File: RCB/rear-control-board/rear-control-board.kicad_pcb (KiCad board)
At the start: 2 copper layers, 99.1 x 99.1 mm, 55 parts, among them J1 Conn_01x23, J2 Conn_01x14, J3 Conn_01x08, J4 Conn_01x02, J5 Conn_01x02, J6 Conn_01x05, K1 T9VV1K15-12S, K2 G5V-2, K3 G5V-2, Q1 BSS84, Q2 2N7002, Q3 Q_PMOS_GDSD, Q4 Q_PMOS_GDSD, Q5 Q_PMOS_GDSD, U1 STM32F413CGUx, U2 LD1117S33TR_SOT223, U3 R-78B5.0-2.0, U4 MCP2551-I-SN, Y1 CSTNE8M00

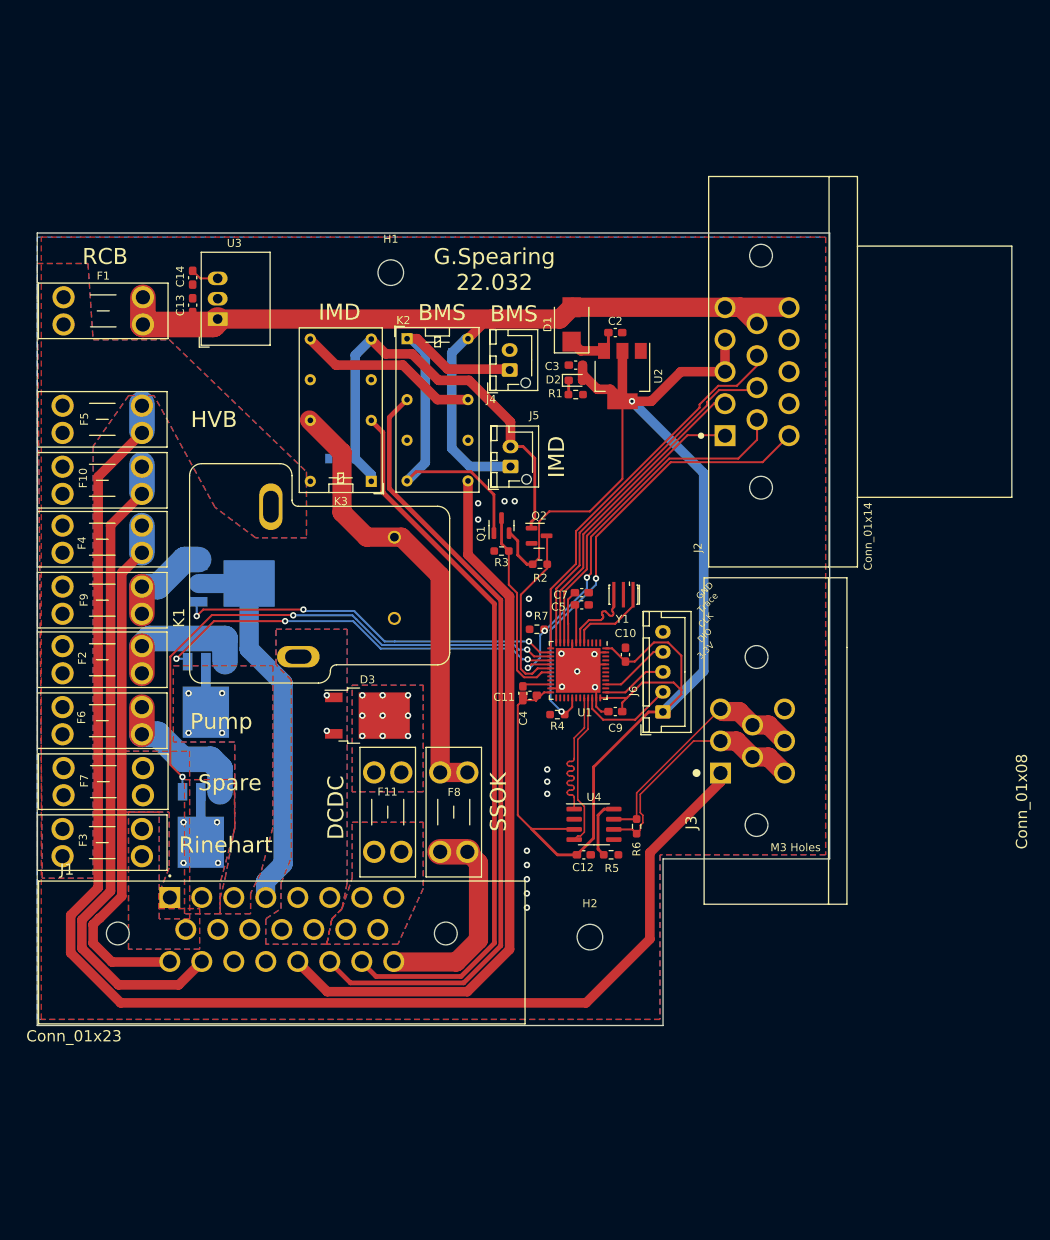
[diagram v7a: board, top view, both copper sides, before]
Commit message: updating schem with design notes (major changes)
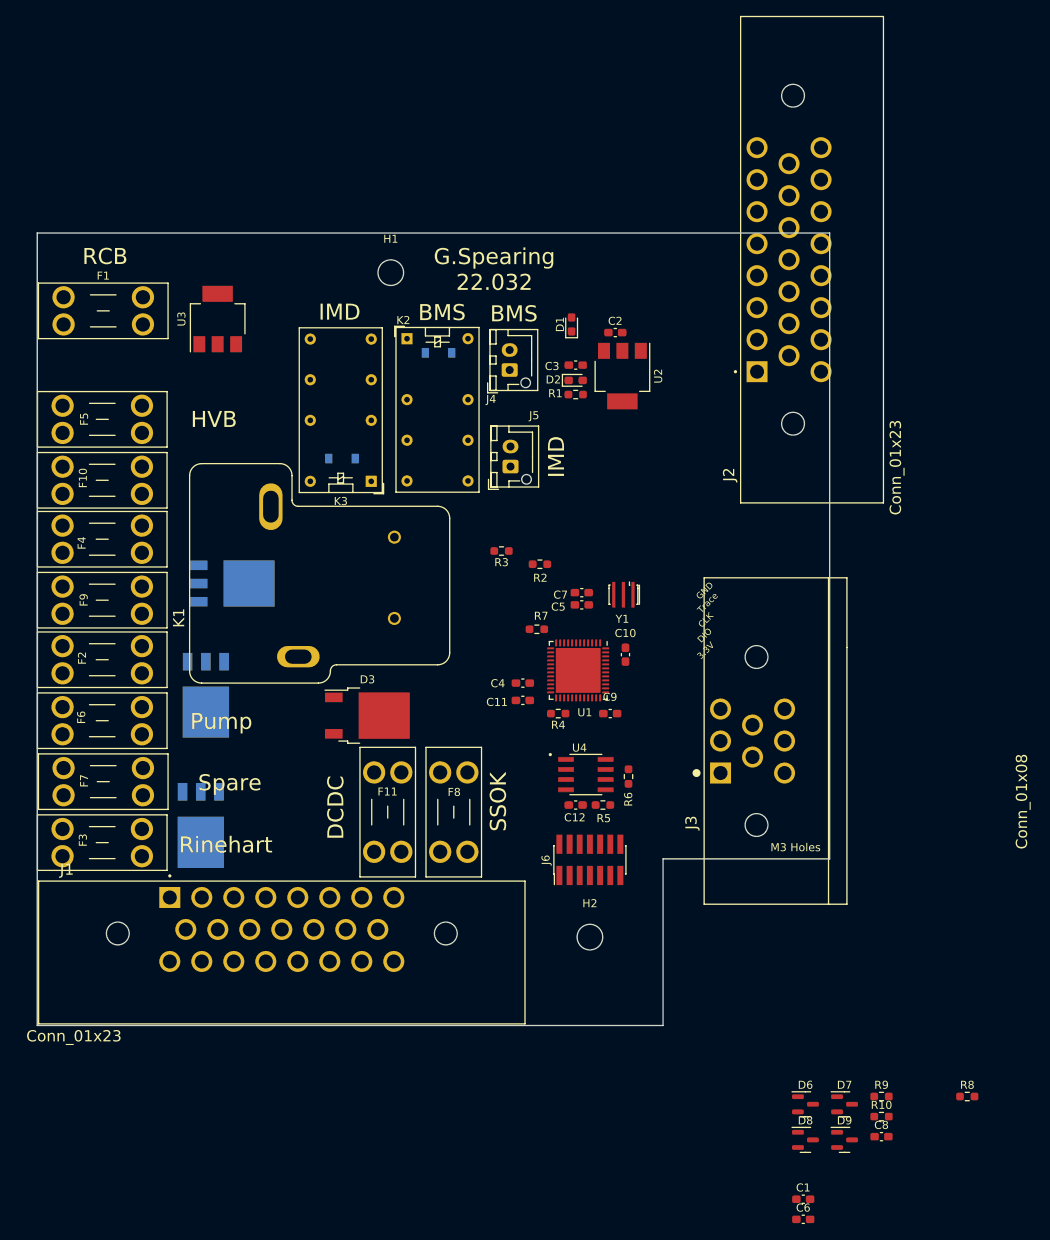
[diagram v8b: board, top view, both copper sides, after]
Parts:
- removed C13: 0.1u, Capacitor_SMD:C_0603_1608Metric_Pad1.08x0.95mm_HandSolder
- removed C14: 10u, Capacitor_SMD:C_0603_1608Metric_Pad1.08x0.95mm_HandSolder
- removed Q1: BSS84, Package_TO_SOT_SMD:SOT-23
- removed Q2: 2N7002, Package_TO_SOT_SMD:SOT-23
- added C1: .1u, Capacitor_SMD:C_0603_1608Metric_Pad1.08x0.95mm_HandSolder, F.Cu at (156.7, 161.4)
- added C6: 10u, Capacitor_SMD:C_0603_1608Metric_Pad1.08x0.95mm_HandSolder, F.Cu at (156.7, 163.9)
- added C8: 0.1u, Capacitor_SMD:C_0603_1608Metric_Pad1.08x0.95mm_HandSolder, F.Cu at (166.5, 153.6)
- added D6: SP0502BAHT, Package_TO_SOT_SMD:SOT-23, F.Cu at (157.0, 149.5)
- added D7: SP0502BAHT, Package_TO_SOT_SMD:SOT-23, F.Cu at (161.9, 149.5)
- added D8: SP0502BAHT, Package_TO_SOT_SMD:SOT-23, F.Cu at (157.0, 154.0)
- added D9: DESD2CAN2SOQ-7, Package_TO_SOT_SMD:SOT-23, F.Cu at (161.9, 154.0)
- added R10: 100, Resistor_SMD:R_0603_1608Metric_Pad0.98x0.95mm_HandSolder, F.Cu at (166.5, 151.1)
- added R8: 2.2K, Resistor_SMD:R_0603_1608Metric_Pad0.98x0.95mm_HandSolder, F.Cu at (177.2, 148.6)
- added R9: 0, Resistor_SMD:R_0603_1608Metric_Pad0.98x0.95mm_HandSolder, F.Cu at (166.5, 148.6)
- D1: value BAT54GW -> LED; footprint Diode_SMD:D_SMB -> LED_SMD:LED_0603_1608Metric_Pad1.05x0.95mm_HandSolder
- F10: value 1A -> 2A
- F9: value 2A -> 1A
- J2: value Conn_01x14 -> Conn_01x23; footprint AERO_Footprints:TE_1-776266-1_14pin_Horizontal -> AERO_Footprints:TE_1-770669-1_23pin_Horizontal
- J4, J5: value Conn_01x02 -> JST-B2B-VERT-2PIN
- J6: value Conn_01x05 -> FTSH-107-01-F-DV-K; footprint Connector_JST:JST_XH_B5B-XH-A_1x05_P2.50mm_Vertical -> Connector_PinHeader_1.27mm:PinHeader_2x07_P1.27mm_Vertical_SMD
- R2: value 10k -> 330
- R4, R7: value 10k -> 1k
- R5: value 1k -> 10K
- U3: value R-78B5.0-2.0 -> LDL1117S33R; footprint Converter_DCDC:Converter_DCDC_RECOM_R-78B-2.0_THT -> Package_TO_SOT_SMD:SOT-223-3_TabPin2
- U4: value MCP2551-I-SN -> MAX33054EASA+T; footprint Package_SO:SOIC-8_3.9x4.9mm_P1.27mm -> AERO_Footprints:SOIC127P600X175-8N
- moved J6 20.6 mm to (130.0, 119.0)
- moved R6 6.31 mm to (134.9, 108.6)
- moved U4 6.31 mm to (129.5, 108.3)
- moved C12 6.31 mm to (128.3, 112.1)
- moved R5 6.31 mm to (131.7, 112.1)
- moved C4 1.27 mm to (121.7, 96.9), turned to 180 degrees
- moved C11 1.09 mm to (121.7, 99.1)
- moved C9 0.68 mm to (132.6, 100.7), turned to 0 degrees
- moved R4 0.16 mm to (126.1, 100.7)
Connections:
- net +12VA renamed /BATT_12V
- net /DASH renamed /FuseBank/FRONT_12V
- net /FAULT_LATCHER/connector renamed Net-(K2-Pad13)
- net /HVB_12V renamed /REAR_12V
- net /RINEHART renamed /FuseBank/RINE_12V
- net /SPARE renamed /FuseBank/SPARE_12V
- C2 pad 1: Net-(C2-Pad1) -> INT_12V
- C7 pad 1: GND -> +3V3
- C7 pad 2: Net-(C7-Pad2) -> GND
- D1 pad 1: Net-(C2-Pad1) -> Net-(D1-Pad1)
- D1 pad 2: VDD -> +3V3
- D4 pad 1: VDD -> INT_12V
- D4 pad 2: /FAULT_LATCHER/bms_switch -> /FAULT_LATCHER/BMS_SWITCH
- D5 pad 1: /FAULT_LATCHER/imd_switch -> /FAULT_LATCHER/IMD_SWITCH
- F1 pad 2: VDD -> INT_12V
- F10 pad 1: +12V -> /SSOK
- F10 pad 2: /BRB -> /FuseBank/TSV
- F8 pad 1: /SSOK -> +12V
- F8 pad 2: /TSV -> /BRAKE_12V
- F9 pad 2: /BRAKE_12V -> /BRB_RTN
- J1 pad 17: /BRB -> /BRB_RTN
- J1 pad 20: /BRB_RTN -> unconnected-(J1-Pad20)
- J1 pad 23: /TSV -> /FuseBank/TSV
- J2 pad 1: /WHEEL_L -> +3V3
- J2 pad 10: /WATER_OUT- -> /WATER_IN-
- J2 pad 11: GND -> +3V3
- J2 pad 12: GND -> +3V3
- J2 pad 13: GND -> /WHEEL_R
- J2 pad 14: VDD -> /WHEEL_L
- J2 pad 2: /WHEEL_R -> +3V3
- J2 pad 5: VDD -> +3V3
- J2 pad 6: /WATER_IN- -> +3V3
- J2 pad 7: /SUSPENSION_L -> /WATER_OUT-
- J2 pad 9: VDD -> /SUSPENSION_L
- J4 pad 1: /FAULT_LATCHER/bms_switch -> /FAULT_LATCHER/BMS_SWITCH
- J5 pad 1: VDD -> INT_12V
- J5 pad 2: /FAULT_LATCHER/imd_switch -> /FAULT_LATCHER/IMD_SWITCH
- J6 pad 1: +3V3 -> unconnected-(J6-Pad1)
- J6 pad 2: A13_SWDIO -> unconnected-(J6-Pad2)
- J6 pad 3: A14_SWCLK -> +3V3
- J6 pad 4: B3_TRACESWO -> A13_SWDIO
- K2 pad 1: /FAULT_LATCHER/bms_switch -> /FAULT_LATCHER/BMS_SWITCH
- K2 pad 16: VDD -> INT_12V
- K2 pad 8: /FAULT_LATCHER/bms_switch -> /FAULT_LATCHER/BMS_SWITCH
- K3 pad 1: /FAULT_LATCHER/imd_switch -> /FAULT_LATCHER/IMD_SWITCH
- K3 pad 8: /FAULT_LATCHER/imd_switch -> /FAULT_LATCHER/IMD_SWITCH
- R2 pad 1: +3V3 -> GND
- R2 pad 2: /Controller/FAULT_IMD -> Net-(D1-Pad1)
- R3 pad 1: /Controller/FAULT_BMS -> +3V3
- R3 pad 2: GND -> /FAULT_LATCHER/BMS_SWITCH
- R5 pad 1: Net-(R5-Pad1) -> /FAULT_LATCHER/IMD_SWITCH
- R5 pad 2: GND -> /Controller/FAULT_IMD
- U1 pad 19: /Controller/FAULT_BMS -> /FAULT_LATCHER/BMS_SWITCH
- U1 pad 32: /Controller/CAN_X_P -> /Controller/CAN_RX
- U1 pad 33: /Controller/CAN_X_N -> /Controller/CAN_TX
- U1 pad 44: GND -> Net-(U1-Pad44)
- U1 pad 9: Net-(C7-Pad2) -> +3V3
- U2 pad 3: Net-(C2-Pad1) -> INT_12V
- U3 pad 1: VDD -> GND
- U3 pad 2: GND -> +3V3
- U3 pad 3: +5V -> INT_12V
- U4 pad 1: /Controller/CAN_X_P -> /Controller/CAN_TX
- U4 pad 4: /Controller/CAN_X_N -> /Controller/CAN_RX
- U4 pad 5: unconnected-(U4-Pad5) -> +3V3
- U4 pad 8: Net-(R5-Pad1) -> GND
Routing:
- net +3V3: track 201.0 -> 0.00 mm, vias 1 -> 0
- net /REAR_12V: track 174.8 -> 0.00 mm
- net VDD: track 117.7 -> 0.00 mm
- net /FAULT_IMD: track 99.4 -> 0.00 mm
- net /BRB_RTN: track 90.9 -> 0.00 mm
- net /FAULT_BMS: track 90.9 -> 0.00 mm
- net /BRB: track 81.3 -> 0.00 mm
- net /Controller/PUMP_CTRL: track 69.4 -> 0.00 mm, vias 3 -> 0
- net /FuseBank/FRONT_12V: track 65.2 -> 0.00 mm
- net /WATER_OUT-: track 57.2 -> 0.00 mm, vias 2 -> 0
- net /FAULT_LATCHER/imd_switch: track 56.9 -> 0.00 mm
- net /SSOK: track 56.8 -> 0.00 mm
- net /FAULT_LATCHER/bms_switch: track 51.8 -> 0.00 mm
- net /Controller/FAN_CTRL: track 51.8 -> 0.00 mm, vias 3 -> 0
- net /WATER_IN-: track 51.1 -> 0.00 mm, vias 3 -> 0
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- removed copper zone on B.Cu, net +12V
- removed copper zone on F.Cu, net +12V
- removed copper zone on B.Cu, net /BATT_12V
- removed copper zone on F.Cu, net /BATT_12V
- removed copper zone on B.Cu, net /DCDC_IN
- removed copper zone on F.Cu, net /DCDC_IN
- removed copper zone on B.Cu, net /FAN_CTRL_12V
- removed copper zone on F.Cu, net /FAN_CTRL_12V
- removed copper zone on B.Cu, net /FuseBank/RINE_12V
- removed copper zone on F.Cu, net /FuseBank/RINE_12V
- removed copper zone on B.Cu, net /FuseBank/SPARE_12V
- removed copper zone on F.Cu, net /FuseBank/SPARE_12V
- removed copper zone on B.Cu, net /PUMP_CTRL_12V
- removed copper zone on F.Cu, net /PUMP_CTRL_12V
- removed copper zone on B.Cu, net /charge-controller/dcdc_fuse
- removed copper zone on F.Cu, net /charge-controller/dcdc_fuse
- removed copper zone on B.Cu, net GND
- removed copper zone on F.Cu, net GND
